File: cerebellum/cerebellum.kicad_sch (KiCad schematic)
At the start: 6 parts, among them J1 GPIO, U1 CAT24C256

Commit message: update design
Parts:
- added A1: RaspberryPi_Pico, Module:RaspberryPi_Pico_Common_THT, symbol RaspberryPi_Pico:RaspberryPi_Pico
- added U2: POLOLU_TB6612_CARRIER, POLOLU_TB6612:POLOLU_TB6612, symbol POLOLU_TB6612:POLOLU-713
- C1: footprint (none) -> POLOLU_TB6612:POLOLU_TB6612
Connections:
- net GPIO2/SDA1 renamed SDA
- net GPIO3/SCL1 renamed SCL
- new net: A1.13 (GND), A1.18 (GND), A1.23 (GND), A1.28 (GND), A1.3 (GND), A1.38 (GND), A1.8 (GND)
- new net: U2.1 (GND), U2.8 (GND), U2.9 (GND)
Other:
- moved on the sheet: J1

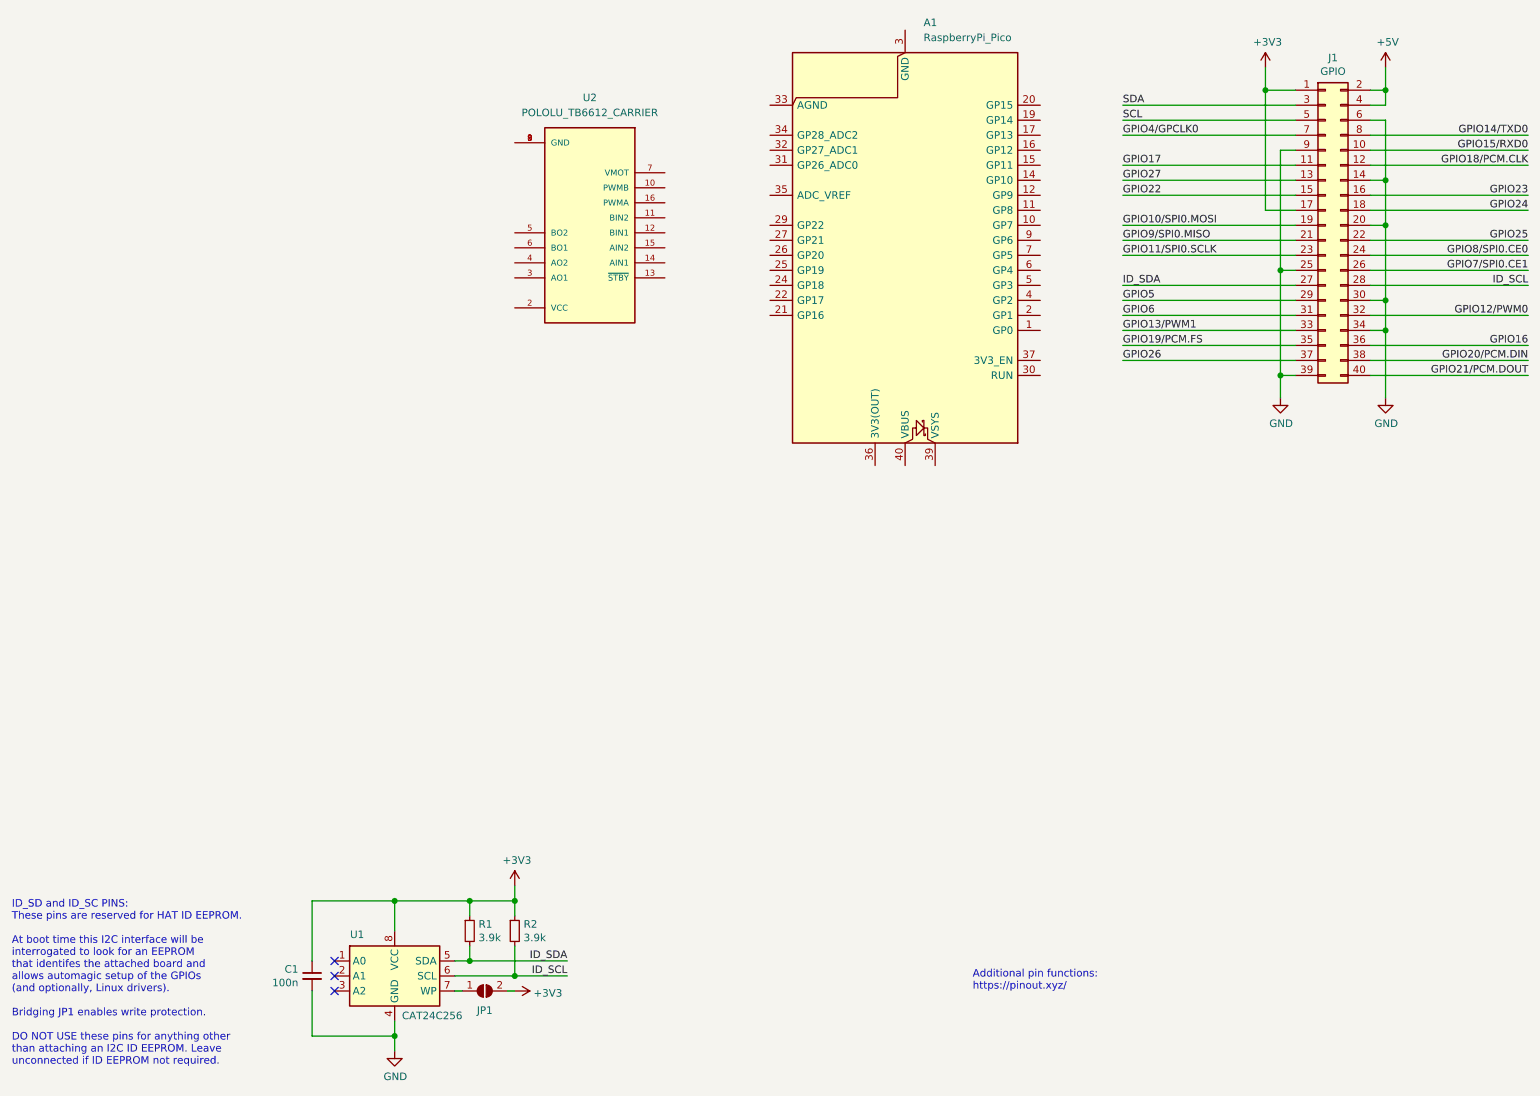
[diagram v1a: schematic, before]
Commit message: label comm pins
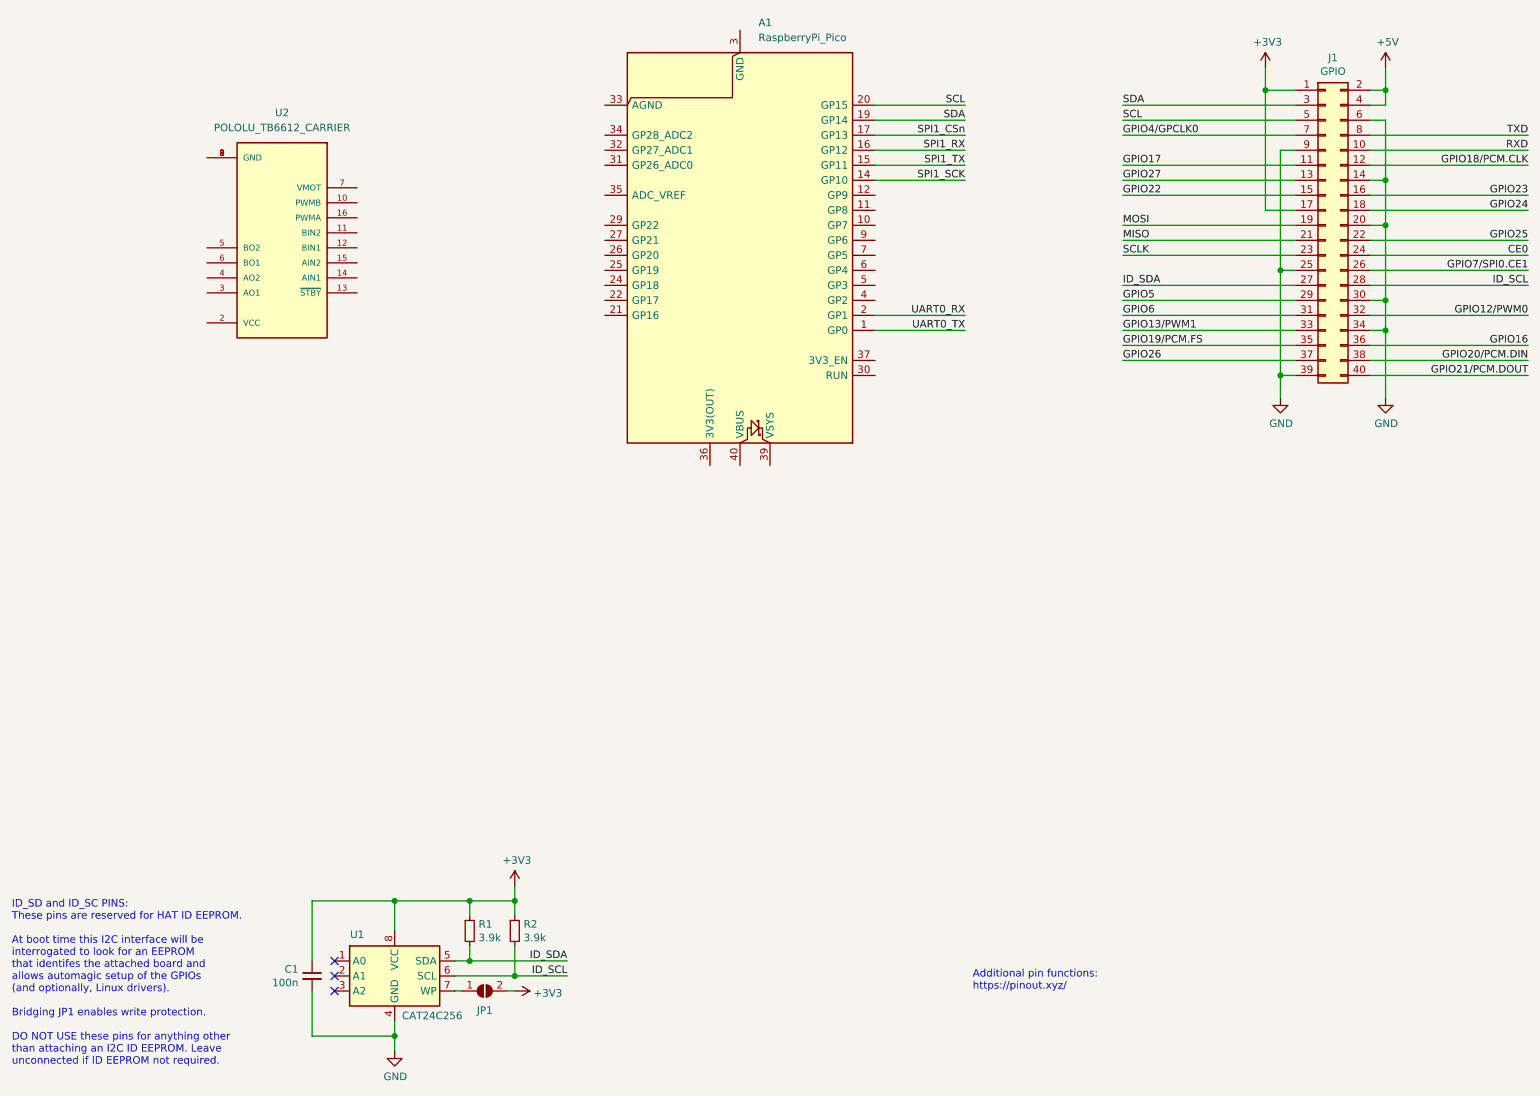
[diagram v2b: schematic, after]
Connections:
- net SCL: now also A1.20 (GP15)
- net SDA: now also A1.19 (GP14)
- net UART0_TX: now reaches A1.1 (GP0)
- net SPI1_SCK: now reaches A1.14 (GP10)
- net SPI1_TX: now reaches A1.15 (GP11)
- net SPI1_RX: now reaches A1.16 (GP12)
- net SPI1_CSn: now reaches A1.17 (GP13)
- net UART0_RX: now reaches A1.2 (GP1)
- net GPIO10/SPI0.MOSI renamed MOSI
- net GPIO11/SPI0.SCLK renamed SCLK
- net GPIO14/TXD0 renamed TXD
- net GPIO15/RXD0 renamed RXD
- net GPIO8/SPI0.CE0 renamed CE0
- net GPIO9/SPI0.MISO renamed MISO
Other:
- moved on the sheet: A1, U2
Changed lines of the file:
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@@
+	(wire
+		(pts
+			(xy 162.56 43.18) (xy 177.8 43.18)
+		)
+		(stroke
+			(width 0)
+			(type default)
+		)
+	)
 	(wire
 		(pts
@@
 	(wire
 		(pts
+			(xy 162.56 38.1) (xy 177.8 38.1)
+		)
+		(stroke
+			(width 0)
+			(type default)
+		)
+	)
+	(wire
+		(pts
 			(xy 248.92 68.58) (xy 246.38 68.58)
 		)
@@
 	(wire
 		(pts
+			(xy 162.56 30.48) (xy 177.8 30.48)
+		)
+		(stroke
+			(width 0)
+			(type default)
+		)
+	)
+	(wire
+		(pts
 			(xy 204.47 55.88) (xy 233.68 55.88)
 		)
@@
 	(wire
 		(pts
+			(xy 162.56 35.56) (xy 177.8 35.56)
+		)
+		(stroke
+			(width 0)
+			(type default)
+		)
+	)
+	(wire
+		(pts
 			(xy 204.47 71.12) (xy 233.68 71.12)
 		)
@@
 	(wire
 		(pts
+			(xy 162.56 40.64) (xy 177.8 40.64)
+		)
+		(stroke
+			(width 0)
+			(type default)
+		)
+	)
+	(wire
+		(pts
 			(xy 248.92 63.5) (xy 246.38 63.5)
 		)
@@
 	(wire
 		(pts
+			(xy 162.56 33.02) (xy 177.8 33.02)
+		)
+		(stroke
+			(width 0)
+			(type default)
+		)
+	)
+	(wire
+		(pts
 			(xy 228.6 27.94) (xy 233.68 27.94)
 		)
@@
 			(width 0)
 			(type solid)
+		)
+	)
+	(wire
+		(pts
+			(xy 162.56 68.58) (xy 177.8 68.58)
+		)
+		(stroke
+			(width 0)
+			(type default)
+		)
+	)
+	(wire
+		(pts
+			(xy 162.56 66.04) (xy 177.8 66.04)
+		)
+		(stroke
+			(width 0)
+			(type default)
 		)
 	)
@@
 		)
 	)
+	(label "SDA"
+		(at 177.8 33.02 180)
+		(effects
+			(font
+				(size 1.27 1.27)
+			)
+			(justify right bottom)
+		)
+	)
 	(label "ID_SDA"
 		(at 110.49 175.26 180)
@@
 		)
 	)
-	(label "GPIO10{slash}SPI0.MOSI"
+	(label "MOSI"
 		(at 204.47 50.8 0)
 		(effects
@@
 		)
 	)
-	(label "GPIO9{slash}SPI0.MISO"
+	(label "MISO"
 		(at 204.47 53.34 0)
 		(effects
@@
 		)
 	)
-	(label "GPIO14{slash}TXD0"
+	(label "TXD"
 		(at 273.05 35.56 180)
 		(effects
@@
 		)
 	)
-	(label "GPIO8{slash}SPI0.CE0"
+	(label "CE0"
 		(at 273.05 55.88 180)
 		(effects
@@
 		)
 	)
-	(label "GPIO15{slash}RXD0"
+	(label "RXD"
 		(at 273.05 38.1 180)
 		(effects
@@
 		)
 	)
+	(label "SPI1_SCK"
+		(at 177.8 43.18 180)
+		(effects
+			(font
+				(size 1.27 1.27)
+			)
+			(justify right bottom)
+		)
+	)
+	(label "SPI1_CSn"
+		(at 177.8 35.56 180)
+		(effects
+			(font
+				(size 1.27 1.27)
+			)
+			(justify right bottom)
+		)
+	)
 	(label "GPIO22"
 		(at 204.47 45.72 0)
@@
 		)
 	)
+	(label "UART0_TX"
+		(at 177.8 68.58 180)
+		(effects
+			(font
+				(size 1.27 1.27)
+			)
+			(justify right bottom)
+		)
+	)
 	(label "GPIO13{slash}PWM1"
 		(at 204.47 68.58 0)
@@
 		)
 	)
+	(label "UART0_RX"
+		(at 177.8 66.04 180)
+		(effects
+			(font
+				(size 1.27 1.27)
+			)
+			(justify right bottom)
+		)
+	)
 	(label "GPIO24"
 		(at 273.05 48.26 180)
@@
 		)
 	)
+	(label "SCL"
+		(at 177.8 30.48 180)
+		(effects
+			(font
+				(size 1.27 1.27)
+			)
+			(justify right bottom)
+		)
+	)
+	(label "SPI1_TX"
+		(at 177.8 40.64 180)
+		(effects
+			(font
+				(size 1.27 1.27)
+			)
+			(justify right bottom)
+		)
+	)
 	(label "ID_SCL"
 		(at 110.49 177.8 180)
@@
 		)
 	)
-	(label "GPIO11{slash}SPI0.SCLK"
+	(label "SPI1_RX"
+		(at 177.8 38.1 180)
+		(effects
+			(font
+				(size 1.27 1.27)
+			)
+			(justify right bottom)
+		)
+	)
+	(label "SCLK"
 		(at 204.47 55.88 0)
 		(effects
@@
 	(symbol
 		(lib_id "RaspberryPi_Pico:RaspberryPi_Pico")
-		(at 167.64 53.34 180)
+		(at 139.7 53.34 180)
 		(unit 1)
 		(exclude_from_sim no)
@@
 		(fields_autoplaced yes)
 		(property "Reference" "A1"
-			(at 170.7581 16.51 0)
+			(at 142.8181 16.51 0)
 			(effects
 				(font
@@
 		)
 		(property "Value" "RaspberryPi_Pico"
-			(at 170.7581 19.05 0)
+			(at 142.8181 19.05 0)
 			(effects
 				(font
@@
 		)
 		(property "Footprint" "Module:RaspberryPi_Pico_Common_THT"
-			(at 167.64 6.35 0)
+			(at 139.7 6.35 0)
 			(effects
 				(font
@@
 		)
 		(property "Datasheet" "https://datasheets.raspberrypi.com/pico/pico-datasheet.pdf"
-			(at 167.64 3.81 0)
+			(at 139.7 3.81 0)
 			(effects
 				(font
@@
 		)
 		(property "Description" "Versatile and inexpensive microcontroller module powered by RP2040 dual-core Arm Cortex-M0+ processor up to 133 MHz, 264kB SRAM, 2MB QSPI flash; also supports Raspberry Pi Pico 2"
-			(at 167.64 1.27 0)
+			(at 139.7 1.27 0)
 			(effects
 				(font
@@
 	(symbol
 		(lib_id "POLOLU_TB6612:POLOLU-713")
-		(at 114.3 52.07 180)
+		(at 62.23 54.61 180)
 		(unit 1)
 		(exclude_from_sim no)
@@
 		(fields_autoplaced yes)
 		(property "Reference" "U2"
-			(at 114.3 29.21 0)
+			(at 62.23 31.75 0)
 			(effects
 				(font
@@
 		)
 		(property "Value" "POLOLU_TB6612_CARRIER"
-			(at 114.3 31.75 0)
+			(at 62.23 34.29 0)
 			(effects
 				(font
@@
 		)
 		(property "Footprint" "POLOLU_TB6612:POLOLU_TB6612"
-			(at 114.3 52.07 0)
+			(at 62.23 54.61 0)
 			(effects
 				(font
@@
 		)
 		(property "Datasheet" ""
-			(at 114.3 52.07 0)
+			(at 62.23 54.61 0)
 			(effects
 				(font
@@
 		)
 		(property "Description" ""
-			(at 114.3 52.07 0)
+			(at 62.23 54.61 0)
 			(effects
 				(font
@@
 		)
 		(property "MF" "Pololu"
-			(at 114.3 52.07 0)
+			(at 62.23 54.61 0)
 			(effects
 				(font
@@
 		)
 		(property "Description_1" "DC-motor driver; IC: TB6612FNG; 100kHz; 1A; Uin mot: 4.5"
-			(at 114.3 52.07 0)
+			(at 62.23 54.61 0)
 			(effects
 				(font
@@
 		)
 		(property "Package" "None"
-			(at 114.3 52.07 0)
+			(at 62.23 54.61 0)
 			(effects
 				(font
@@
 		)
 		(property "Price" "None"
-			(at 114.3 52.07 0)
+			(at 62.23 54.61 0)
 			(effects
 				(font
@@
 		)
 		(property "Check_prices" "https://www.snapeda.com/parts/POLOLU-713/Pololu/view-part/?ref=eda"
-			(at 114.3 52.07 0)
+			(at 62.23 54.61 0)
 			(effects
 				(font
@@
 		)
 		(property "STANDARD" "Manufacturer recommendations"
-			(at 114.3 52.07 0)
+			(at 62.23 54.61 0)
 			(effects
 				(font
@@
 		)
 		(property "PARTREV" ""
-			(at 114.3 52.07 0)
+			(at 62.23 54.61 0)
 			(effects
 				(font
@@
 		)
 		(property "SnapEDA_Link" "https://www.snapeda.com/parts/POLOLU-713/Pololu/view-part/?ref=snap"
-			(at 114.3 52.07 0)
+			(at 62.23 54.61 0)
 			(effects
 				(font
@@
 		)
 		(property "MP" "POLOLU-713"
-			(at 114.3 52.07 0)
+			(at 62.23 54.61 0)
 			(effects
 				(font
@@
 		)
 		(property "Availability" "Not in stock"
-			(at 114.3 52.07 0)
+			(at 62.23 54.61 0)
 			(effects
 				(font
@@
 		)
 		(property "MANUFACTURER" "POLOLU"
-			(at 114.3 52.07 0)
-			(effects
-				(font
+			(at 62.23 54.61 0)
+			(effects
+				(font

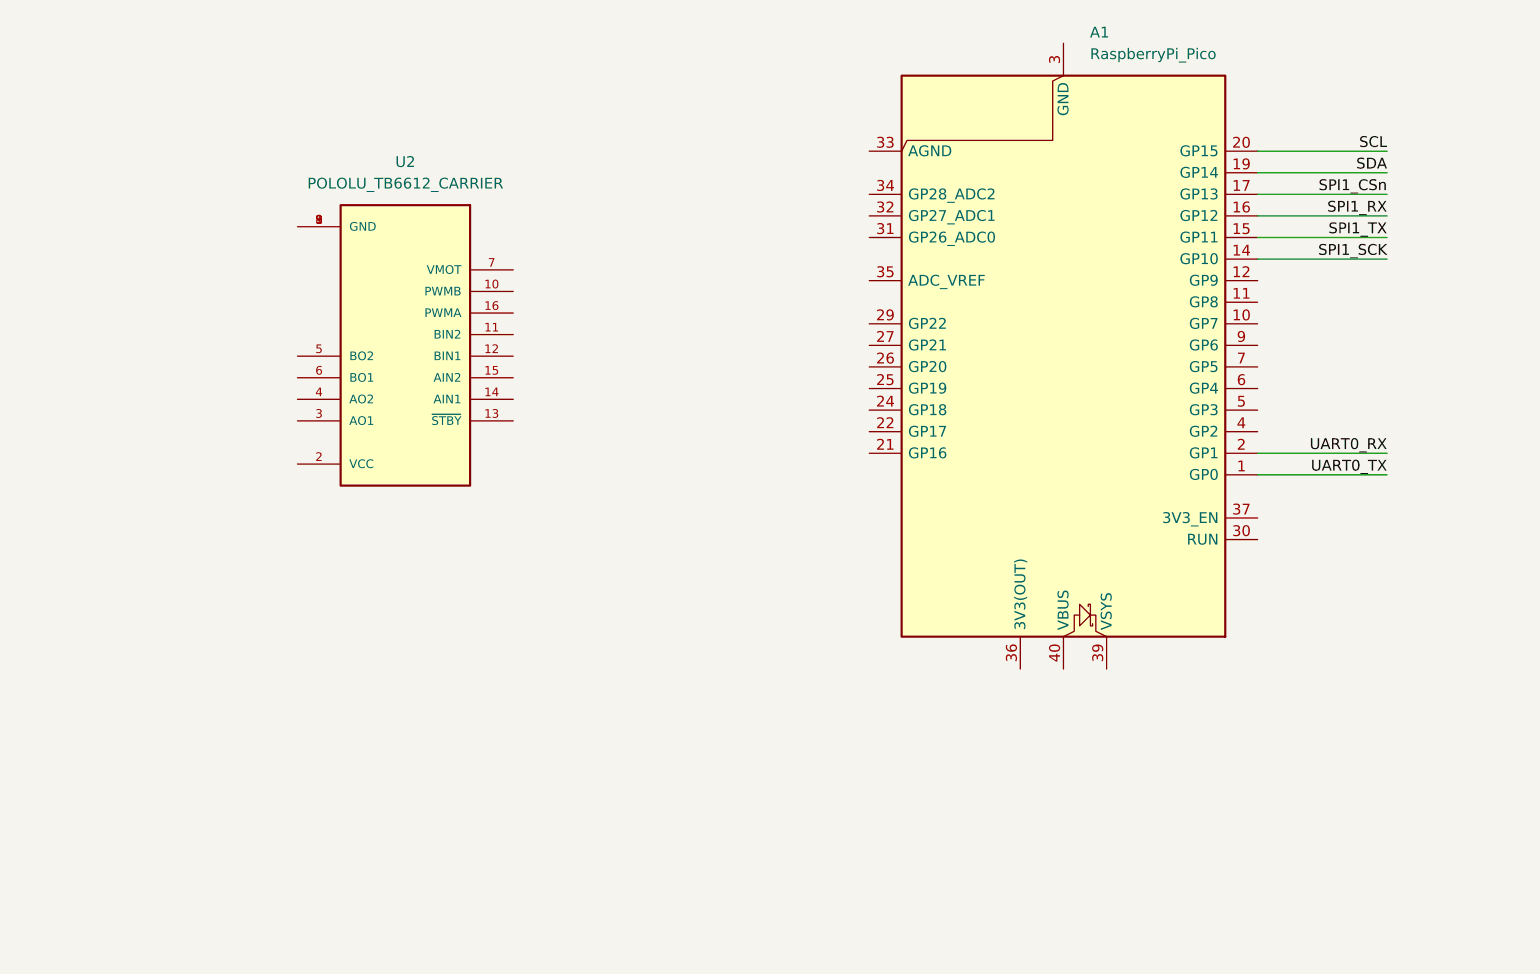
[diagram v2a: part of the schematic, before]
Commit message: update schematic
assign labels to pico
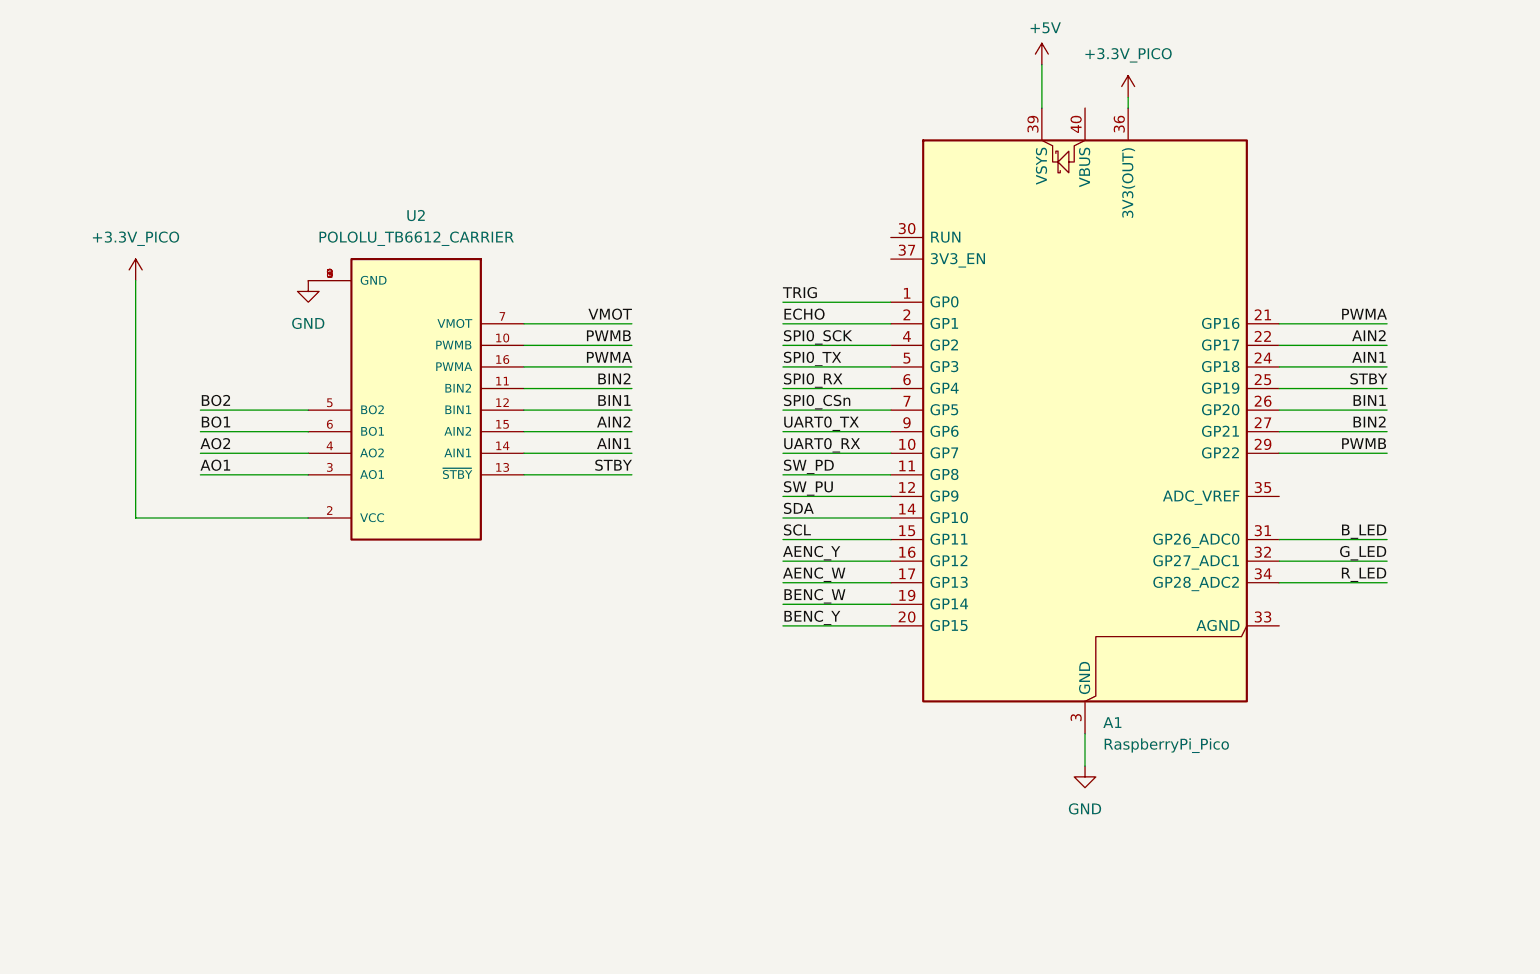
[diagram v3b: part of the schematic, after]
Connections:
- net SPI1_SCK is gone; now on net SDA: A1.14 (GP10)
- net SPI1_TX is gone; now on net SCL: A1.15 (GP11)
- net +5V: now also A1.39 (VSYS)
- net GND: now also A1.13 (GND), A1.18 (GND), A1.23 (GND), A1.28 (GND), A1.3 (GND), A1.38 (GND), A1.8 (GND), U2.1 (GND), U2.8 (GND), U2.9 (GND)
- net SCL: no longer A1.20 (GP15)
- net SDA: no longer A1.19 (GP14)
- net UART0_RX: now also A1.10 (GP7); no longer A1.2 (GP1)
- net UART0_TX: now also A1.9 (GP6); no longer A1.1 (GP0)
- net SW_PD: now reaches A1.11 (GP8)
- net SW_PU: now reaches A1.12 (GP9)
- net PWMA: now reaches A1.21 (GP16)
- net PWMA: now also U2.16 (PWMA)
- net AIN2: now reaches A1.22 (GP17)
- net AIN2: now also U2.15 (AIN2)
- net AIN1: now reaches A1.24 (GP18)
- net AIN1: now also U2.14 (AIN1)
- net STBY: now reaches A1.25 (GP19)
- net STBY: now also U2.13 (~{STBY})
- net BIN1: now reaches A1.26 (GP20)
- net BIN1: now also U2.12 (BIN1)
- net BIN2: now reaches A1.27 (GP21)
- net BIN2: now also U2.11 (BIN2)
- net PWMB: now reaches A1.29 (GP22)
- net PWMB: now also U2.10 (PWMB)
- net B_LED: now reaches A1.31 (GP26_ADC0)
- net G_LED: now reaches A1.32 (GP27_ADC1)
- net R_LED: now reaches A1.34 (GP28_ADC2)
- net +3.3V_PICO: now reaches A1.36 (3V3(OUT))
- net +3.3V_PICO: now also U2.2 (VCC)
- net SPI0_SCK: now reaches A1.4 (GP2)
- net SPI0_TX: now reaches A1.5 (GP3)
- net SPI0_RX: now reaches A1.6 (GP4)
- net SPI0_CSn: now reaches A1.7 (GP5)
- net AO1: now reaches U2.3 (AO1)
- net AO2: now reaches U2.4 (AO2)
- net BO2: now reaches U2.5 (BO2)
- net BO1: now reaches U2.6 (BO1)
- net VMOT: now reaches U2.7 (VMOT)
- net SPI1_CSn renamed AENC_W
- net SPI1_RX renamed AENC_Y
- new net BENC_W: A1.19 (GP14)
- new net BENC_Y: A1.20 (GP15)
- new net ECHO: A1.2 (GP1)
- new net TRIG: A1.1 (GP0)
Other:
- moved on the sheet: A1, U2
